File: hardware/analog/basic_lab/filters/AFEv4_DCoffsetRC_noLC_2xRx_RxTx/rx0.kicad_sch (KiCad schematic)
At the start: 7 parts

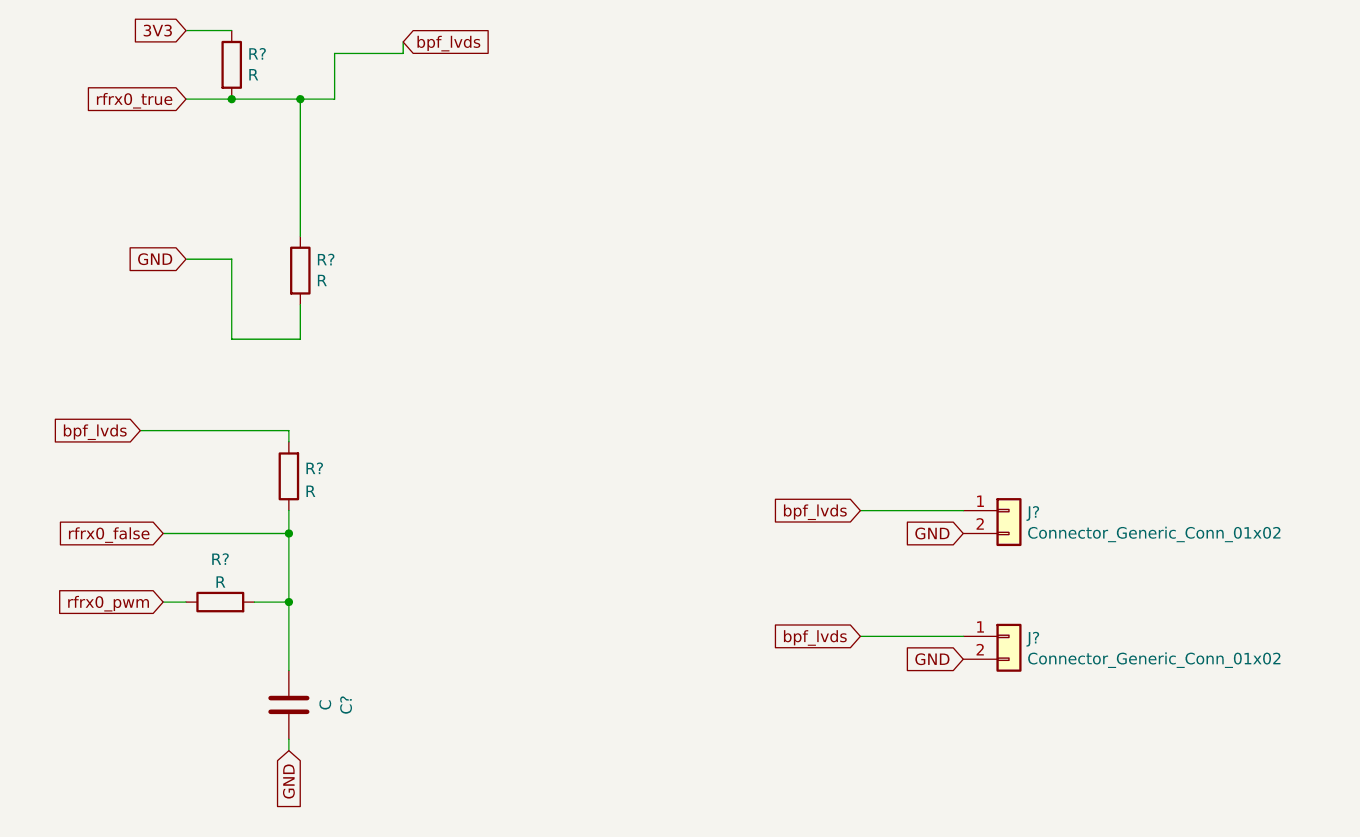
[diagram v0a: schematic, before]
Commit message: started 2xRx / RxTx PCBs with no / simple LC filters
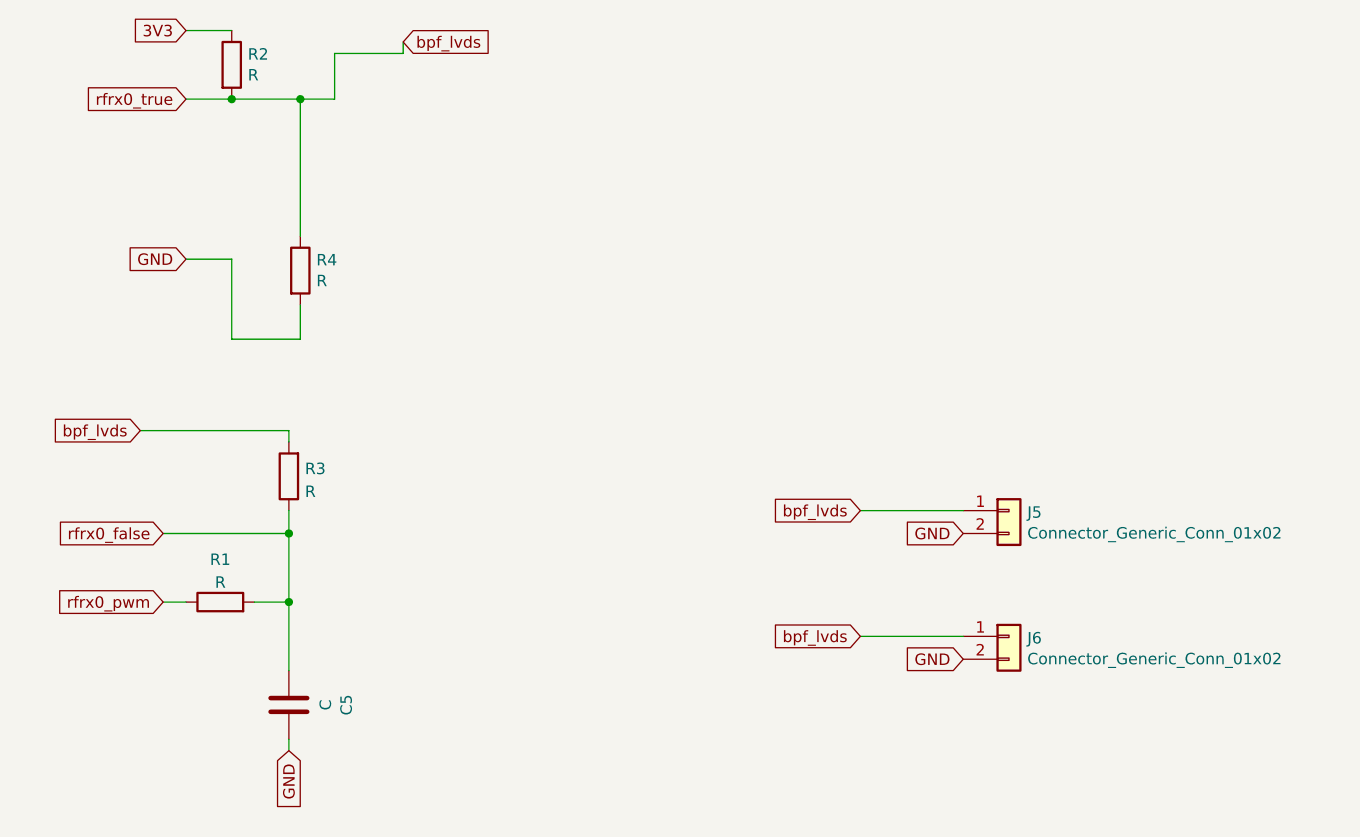
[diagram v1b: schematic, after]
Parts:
- gave numbers to parts that had none: 7
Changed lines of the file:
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@@
   (symbol (lib_id "Device:C") (at 99.06 105.41 180) (unit 1)
     (in_bom yes) (on_board yes)
-    (property "Reference" "C?" (id 0) (at 105.4608 105.41 90))
+    (property "Reference" "C5" (id 0) (at 105.4608 105.41 90))
     (property "Value" "C" (id 1) (at 103.1494 105.41 90))
     (property "Footprint" "Capacitor_THT:C_Axial_L3.8mm_D2.6mm_P7.50mm_Horizontal" (id 2) (at 98.0948 101.6 0)
@@
   (symbol (lib_id "Device:R") (at 92.71 34.29 0) (unit 1)
     (in_bom yes) (on_board yes)
-    (property "Reference" "R?" (id 0) (at 94.488 33.1216 0)
+    (property "Reference" "R2" (id 0) (at 94.488 33.1216 0)
       (effects (font (size 1.27 1.27)) (justify left))
     )
@@
   (symbol (lib_id "Device:R") (at 100.33 57.15 0) (unit 1)
     (in_bom yes) (on_board yes)
-    (property "Reference" "R?" (id 0) (at 102.108 55.9816 0)
+    (property "Reference" "R4" (id 0) (at 102.108 55.9816 0)
       (effects (font (size 1.27 1.27)) (justify left))
     )
@@
   (symbol (lib_id "Device:R") (at 91.44 93.98 90) (unit 1)
     (in_bom yes) (on_board yes) (fields_autoplaced)
-    (property "Reference" "R?" (id 0) (at 91.44 89.2642 90))
+    (property "Reference" "R1" (id 0) (at 91.44 89.2642 90))
     (property "Value" "R" (id 1) (at 91.44 91.8011 90))
     (property "Footprint" "Resistor_THT:R_Axial_DIN0207_L6.3mm_D2.5mm_P5.08mm_Vertical" (id 2) (at 91.44 95.758 90)
@@
   (symbol (lib_id "bgt:Connector_Generic_Conn_01x02") (at 179.07 83.82 0) (unit 1)
     (in_bom yes) (on_board yes)
-    (property "Reference" "J?" (id 0) (at 181.102 84.0232 0)
+    (property "Reference" "J5" (id 0) (at 181.102 84.0232 0)
       (effects (font (size 1.27 1.27)) (justify left))
     )
@@
   (symbol (lib_id "Device:R") (at 99.06 80.01 180) (unit 1)
     (in_bom yes) (on_board yes) (fields_autoplaced)
-    (property "Reference" "R?" (id 0) (at 100.838 79.1753 0)
+    (property "Reference" "R3" (id 0) (at 100.838 79.1753 0)
       (effects (font (size 1.27 1.27)) (justify right))
     )
@@
   (symbol (lib_id "bgt:Connector_Generic_Conn_01x02") (at 179.07 97.79 0) (unit 1)
     (in_bom yes) (on_board yes)
-    (property "Reference" "J?" (id 0) (at 181.102 97.9932 0)
+    (property "Reference" "J6" (id 0) (at 181.102 97.9932 0)
       (effects (font (size 1.27 1.27)) (justify left))
     )

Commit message: started 2xRx / RxTx PCBs with no / simple LC filters: Gerber with THT board; started SMD board in the same DIR
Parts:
- C5: footprint Capacitor_THT:C_Axial_L3.8mm_D2.6mm_P7.50mm_Horizontal -> Capacitor_SMD:C_1206_3216Metric
- R1, R2, R3, R4: footprint Resistor_THT:R_Axial_DIN0207_L6.3mm_D2.5mm_P5.08mm_Vertical -> Resistor_SMD:R_1206_3216Metric
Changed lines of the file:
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@@
     (property "Reference" "C5" (id 0) (at 105.4608 105.41 90))
     (property "Value" "C" (id 1) (at 103.1494 105.41 90))
-    (property "Footprint" "Capacitor_THT:C_Axial_L3.8mm_D2.6mm_P7.50mm_Horizontal" (id 2) (at 98.0948 101.6 0)
+    (property "Footprint" "Capacitor_SMD:C_1206_3216Metric" (id 2) (at 98.0948 101.6 0)
       (effects (font (size 1.27 1.27)) hide)
     )
@@
       (effects (font (size 1.27 1.27)) (justify left))
     )
-    (property "Footprint" "Resistor_THT:R_Axial_DIN0207_L6.3mm_D2.5mm_P5.08mm_Vertical" (id 2) (at 90.932 34.29 90)
+    (property "Footprint" "Resistor_SMD:R_1206_3216Metric" (id 2) (at 90.932 34.29 90)
       (effects (font (size 1.27 1.27)) hide)
     )
@@
       (effects (font (size 1.27 1.27)) (justify left))
     )
-    (property "Footprint" "Resistor_THT:R_Axial_DIN0207_L6.3mm_D2.5mm_P5.08mm_Vertical" (id 2) (at 98.552 57.15 90)
+    (property "Footprint" "Resistor_SMD:R_1206_3216Metric" (id 2) (at 98.552 57.15 90)
       (effects (font (size 1.27 1.27)) hide)
     )
@@
     (property "Reference" "R1" (id 0) (at 91.44 89.2642 90))
     (property "Value" "R" (id 1) (at 91.44 91.8011 90))
-    (property "Footprint" "Resistor_THT:R_Axial_DIN0207_L6.3mm_D2.5mm_P5.08mm_Vertical" (id 2) (at 91.44 95.758 90)
+    (property "Footprint" "Resistor_SMD:R_1206_3216Metric" (id 2) (at 91.44 95.758 90)
       (effects (font (size 1.27 1.27)) hide)
     )
@@
       (effects (font (size 1.27 1.27)) (justify right))
     )
-    (property "Footprint" "Resistor_THT:R_Axial_DIN0207_L6.3mm_D2.5mm_P5.08mm_Vertical" (id 2) (at 100.838 80.01 90)
+    (property "Footprint" "Resistor_SMD:R_1206_3216Metric" (id 2) (at 100.838 80.01 90)
       (effects (font (size 1.27 1.27)) hide)
     )
